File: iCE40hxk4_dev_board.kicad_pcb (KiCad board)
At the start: 4 copper layers, 66.4 x 162.5 mm, 367 parts, among them J1001 Testpoint, J1002 Testpoint, J1003 Testpoint, J1004 Testpoint, J1005 USB_EXT, J101 CONN_01X02, J102 KobiConn_161-3507_Jack_3.5mm, J103 CONN_COAXIAL, J104 CONN_COAXIAL, J1101 CONN_01X25, J202 USB_OTG, J401 Testpoint, J402 Testpoint, J403 Testpoint, J404 Testpoint, J405 Testpoint, J406 Testpoint, J501 Testpoint, J502 Testpoint, J601 CONN_01X02, J602 CONN_01X02, J603 Testpoint, J604 Testpoint, J605 Testpoint, J701 Testpoint, J702 Testpoint, J703 Testpoint, J704 Testpoint, J705 Testpoint, J706 Testpoint, J801 Testpoint, J802 Testpoint, J803 Testpoint, J804 Testpoint, J805 Testpoint, J806 Testpoint, J807 Testpoint, J808 Testpoint, J809 Testpoint, J810 Testpoint, SW1101 SW_Push, U1001 ADC1175, U1002 ADC1175, U1101 MIC7300, U1102 MIC7300, U1103 MCP4716, U1104 MCP4716, U1105 MIC7300, U1106 MIC7300, U201 MIC2005A-2YM5, U203 93LC56BT-I/O, U204 MIC5355/6-xYMME, U205 FT2232H, U301 iCE40-HX4K-TQ144, U302 25LC_EEPROM, U501 AS4C1M16S, U701 CPC1017N, U702 CPC1017N, U703 CD4051BM96, U704 CD4051BM96, U801 CD4051BM96, U802 CD4051BM96, U803 CLC4007, U901 LM2776DBVR, U902 TCR2EF13, U903 MIC5270

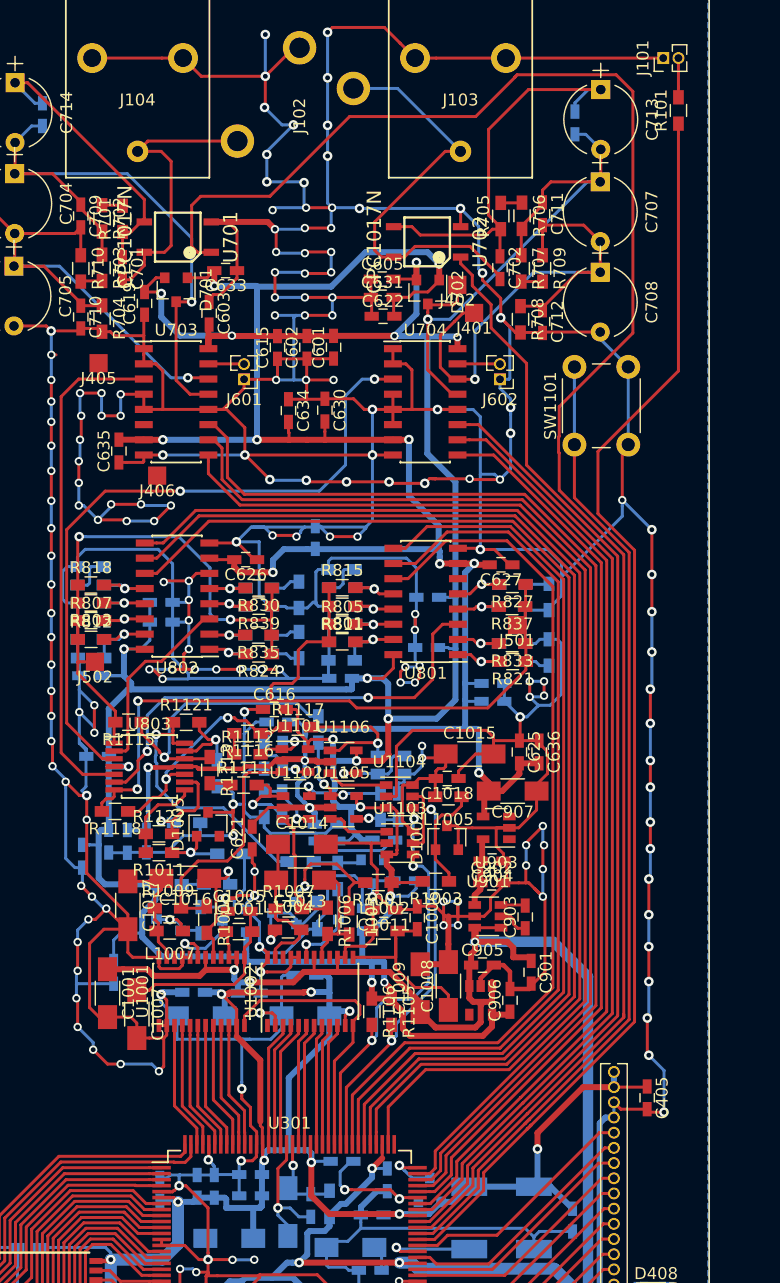
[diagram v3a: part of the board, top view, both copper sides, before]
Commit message: Added resistance to control lines to prevent overshoot
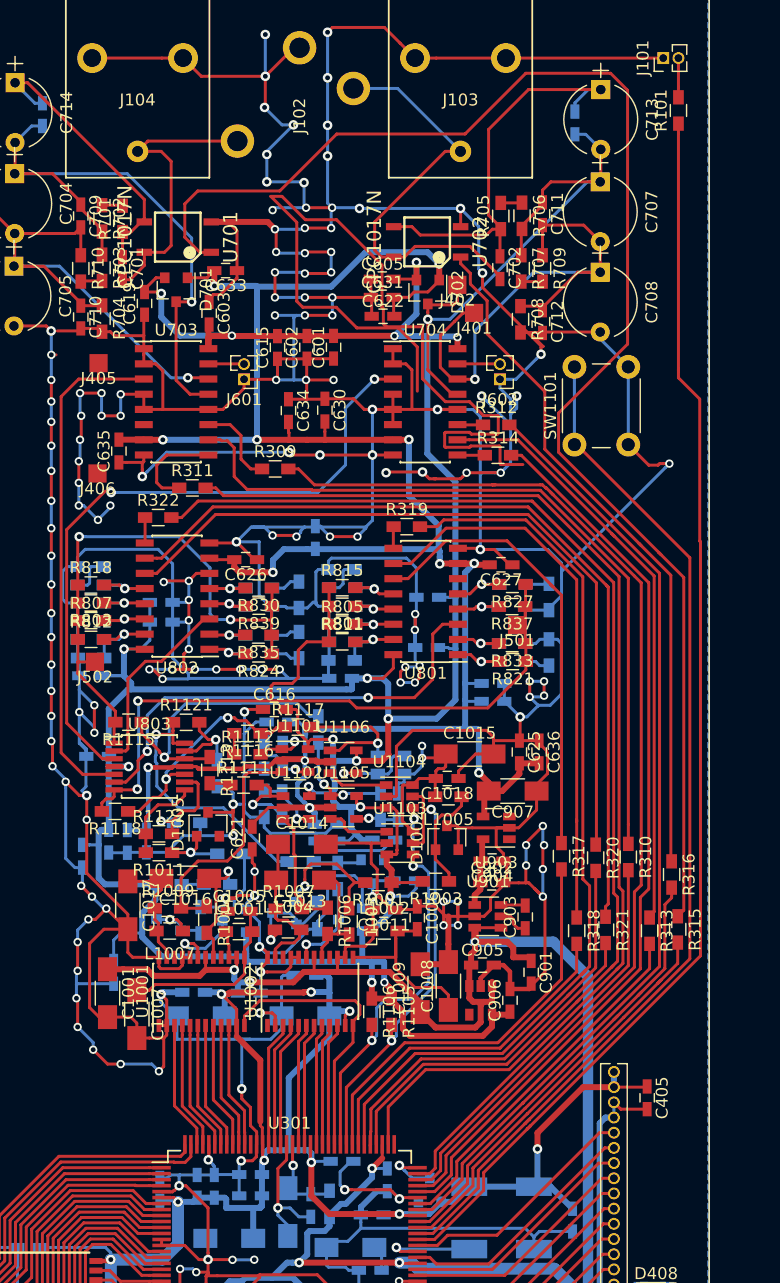
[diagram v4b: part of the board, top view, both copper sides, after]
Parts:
- added R309: 1K, Resistors_SMD:R_0603_HandSoldering, F.Cu at (117.6, 74.3)
- added R310: 1K, Resistors_SMD:R_0603_HandSoldering, F.Cu at (147.2, 106.7)
- added R311: 1K, Resistors_SMD:R_0603_HandSoldering, F.Cu at (110.7, 75.9)
- added R312: 1K, Resistors_SMD:R_0603_HandSoldering, F.Cu at (136.1, 70.6)
- added R313: 1K, Resistors_SMD:R_0603_HandSoldering, F.Cu at (148.9, 112.9)
- added R314: 1K, Resistors_SMD:R_0603_HandSoldering, F.Cu at (136.3, 73.1)
- added R315: 1K, Resistors_SMD:R_0603_HandSoldering, F.Cu at (151.3, 112.8)
- added R316: 1K, Resistors_SMD:R_0603_HandSoldering, F.Cu at (150.8, 108.2)
- added R317: 1K, Resistors_SMD:R_0603_HandSoldering, F.Cu at (141.6, 106.7)
- added R318: 1K, Resistors_SMD:R_0603_HandSoldering, F.Cu at (142.9, 112.9)
- added R319: 1K, Resistors_SMD:R_0603_HandSoldering, F.Cu at (128.6, 79.1)
- added R320: 1K, Resistors_SMD:R_0603_HandSoldering, F.Cu at (144.4, 106.8)
- added R321: 1K, Resistors_SMD:R_0603_HandSoldering, F.Cu at (145.3, 112.8)
- added R322: 1K, Resistors_SMD:R_0603_HandSoldering, F.Cu at (107.9, 78.3)
- moved J406 4.99 mm to (102.8, 74.6)
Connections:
- U701 pad 1: /Analog front end/CHA_DC_COUPLING -> /Analog front end/ATTENUATION/CHA_DC_COUPLING
- U702 pad 1: /Analog front end/CHB_DC_COUPLING -> /Analog front end/ATTENUATION/CHB_DC_COUPLING
- U703 pad 10: /Analog front end/CHA_ATT_SEL_1 -> /Analog front end/ATTENUATION/CHA_ATT_SEL_1
- U703 pad 11: /Analog front end/CHA_ATT_SEL_0 -> /Analog front end/ATTENUATION/CHA_ATT_SEL_0
- U703 pad 9: /Analog front end/CHA_ATT_SEL_2 -> /Analog front end/ATTENUATION/CHA_ATT_SEL_2
- U704 pad 10: /Analog front end/CHB_ATT_SEL_1 -> /Analog front end/ATTENUATION/CHB_ATT_SEL_1
- U704 pad 11: /Analog front end/CHB_ATT_SEL_0 -> /Analog front end/ATTENUATION/CHB_ATT_SEL_0
- U704 pad 9: /Analog front end/CHB_ATT_SEL_2 -> /Analog front end/ATTENUATION/CHB_ATT_SEL_2
- U801 pad 10: /Analog front end/CHA_GAIN_SEL_1 -> /Analog front end/PGA/CHA_GAIN_SEL_1
- U801 pad 11: /Analog front end/CHA_GAIN_SEL_0 -> /Analog front end/PGA/CHA_GAIN_SEL_0
- U801 pad 9: /Analog front end/CHA_GAIN_SEL_2 -> /Analog front end/PGA/CHA_GAIN_SEL_2
- U802 pad 10: /Analog front end/CHB_GAIN_SEL_1 -> /Analog front end/PGA/CHB_GAIN_SEL_1
- U802 pad 11: /Analog front end/CHB_GAIN_SEL_0 -> /Analog front end/PGA/CHB_GAIN_SEL_0
- U802 pad 9: /Analog front end/CHB_GAIN_SEL_2 -> /Analog front end/PGA/CHB_GAIN_SEL_2
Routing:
- net /Analog front end/ATTENUATION/CHA_DC_COUPLING: track 0.00 -> 123.9 mm
- net /Analog front end/CHA_DC_COUPLING: track 155.7 -> 33.9 mm
- net (no net): track 0.00 -> 72.3 mm
- net /Analog front end/PGA/CHB_GAIN_SEL_1: track 0.00 -> 71.6 mm
- net GND: track 1631.9 -> 1560.8 mm, vias 220 -> 197
- net /Analog front end/CHB_GAIN_SEL_1: track 98.5 -> 28.9 mm
- net /Analog front end/PGA/CHB_GAIN_SEL_0: track 0.00 -> 64.5 mm
- net /Analog front end/ATTENUATION/CHA_ATT_SEL_1: track 0.00 -> 63.5 mm
- net /Analog front end/CHB_GAIN_SEL_0: track 98.2 -> 35.2 mm
- net /Analog front end/CHA_ATT_SEL_1: track 95.8 -> 34.0 mm
- net /Analog front end/ATTENUATION/CHB_DC_COUPLING: track 0.00 -> 58.3 mm
- net /Analog front end/CHB_DC_COUPLING: track 93.6 -> 38.1 mm
- net /Analog front end/ATTENUATION/CHB_ATT_SEL_1: track 0.00 -> 50.4 mm
- net /Analog front end/CHB_ATT_SEL_1: track 77.6 -> 30.5 mm
- net /Analog front end/PGA/CHA_GAIN_SEL_1: track 0.00 -> 46.7 mm
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
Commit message: Almost rev1
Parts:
- removed J703, J704: Testpoint, library:TestPoint
- added J105: MountingHole, library:MountingHole, F.Cu at (90.5, 187.0)
- added J106: MountingHole, library:MountingHole, F.Cu at (151.5, 187.0)
- added J107: MountingHole, library:MountingHole, F.Cu at (90.5, 32.0)
- added J108: MountingHole, library:MountingHole, F.Cu at (151.5, 32.0)
- J705, J706, J801, J802, J805, J809, J810: moved to B.Cu
- U203: value 93LC56BT-I/O -> 93LC56BT-I/OT
- U204: value MIC5355/6-xYMME -> MIC5355-S4YMME
- U902: value TCR2EF13 -> TCR2EF13,LM(CT
- moved J403 138.5 mm to (109.3, 62.2)
- moved J702 91.7 mm to (114.9, 108.6)
- moved J808 75.1 mm to (104.2, 105.8)
- moved J807 73.8 mm to (111.6, 93.7)
- moved J1002 70.4 mm to (128.4, 185.9)
- moved J802 68.6 mm to (115.1, 97.9)
- moved J604 66.1 mm to (122.8, 91.3)
- moved J806 65.7 mm to (121.0, 94.2)
- moved J801 62.1 mm to (118.7, 105.0)
- moved J706 61.7 mm to (117.3, 108.9)
- moved J804 58.0 mm to (127.4, 98.5)
- moved J803 56.6 mm to (124.6, 105.6)
- moved J605 56.2 mm to (133.0, 94.6)
- moved J701 55.7 mm to (124.6, 107.4)
- moved J705 54.8 mm to (122.8, 114.0)
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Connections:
- J1005 pad 2: Net-(J1005-Pad2) -> (no net)
- J1005 pad 3: Net-(J1005-Pad3) -> (no net)
- J1005 pad 4: Net-(J1005-Pad4) -> (no net)
- J101 pad 1: GND -> Net-(J101-Pad1)
- J101 pad 2: Net-(J101-Pad2) -> Net-(J101-Pad1)
- J202 pad 4: Net-(J202-Pad4) -> (no net)
- R101 pad 2: Net-(J101-Pad2) -> Net-(J101-Pad1)
- U1001 pad 16: Net-(U1001-Pad16) -> (no net)
- U1001 pad 22: Net-(U1001-Pad22) -> (no net)
- U1002 pad 16: Net-(U1002-Pad16) -> (no net)
- U1002 pad 22: Net-(U1002-Pad22) -> (no net)
- U205 pad 19: Net-(U205-Pad19) -> (no net)
- U205 pad 22: Net-(U205-Pad22) -> (no net)
- U205 pad 26: Net-(U205-Pad26) -> (no net)
- U205 pad 27: Net-(U205-Pad27) -> (no net)
- U205 pad 28: Net-(U205-Pad28) -> (no net)
- U205 pad 29: Net-(U205-Pad29) -> (no net)
- U205 pad 3: Net-(U205-Pad3) -> (no net)
- U205 pad 30: Net-(U205-Pad30) -> (no net)
- U205 pad 32: Net-(U205-Pad32) -> (no net)
- U205 pad 33: Net-(U205-Pad33) -> (no net)
- U205 pad 34: Net-(U205-Pad34) -> (no net)
- U205 pad 36: Net-(U205-Pad36) -> (no net)
- U205 pad 57: Net-(U205-Pad57) -> (no net)
- U205 pad 58: Net-(U205-Pad58) -> (no net)
- U205 pad 59: Net-(U205-Pad59) -> (no net)
- U205 pad 60: Net-(U205-Pad60) -> (no net)
- U301 pad 109: Net-(U301-Pad109) -> (no net)
- U301 pad 133: Net-(U301-Pad133) -> (no net)
- U301 pad 35: Net-(U301-Pad35) -> (no net)
- U301 pad 36: Net-(U301-Pad36) -> (no net)
- U301 pad 50: Net-(U301-Pad50) -> (no net)
- U301 pad 51: Net-(U301-Pad51) -> (no net)
- U301 pad 58: Net-(U301-Pad58) -> (no net)
- U301 pad 77: Net-(U301-Pad77) -> (no net)
- U501 pad 33: Net-(U501-Pad33) -> (no net)
- U501 pad 37: Net-(U501-Pad37) -> (no net)
- U902 pad 4: Net-(U902-Pad4) -> (no net)
- U903 pad 1: Net-(U903-Pad1) -> (no net)
- U903 pad 3: Net-(U903-Pad3) -> (no net)
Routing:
- net (no net): track 72.3 -> 0.00 mm
- net Net-(J101-Pad1): track 0.00 -> 18.6 mm
- net /CHA: track 24.8 -> 37.5 mm
- net /Analog front end/ATTENUATION/CHA_DC_COUPLING: track 123.9 -> 129.5 mm
- net /Analog front end/OFFSET/CHA_V_OFFSET_FIJO: track 4.54 -> 10.0 mm
- net /Analog front end/CHB_OFFSET: track 9.24 -> 14.7 mm
- net /Analog front end/CHB_OFFSET_OUT: track 22.5 -> 27.2 mm
- net /Analog front end/ADC/CHB_V_REF_TOP: track 9.57 -> 13.6 mm
- net /Analog front end/CHB_DC_COUPLING: track 38.1 -> 41.7 mm
- net /Analog front end/-3V0: track 199.1 -> 202.6 mm, vias 12 -> 13
- net /USB+OSCILLATOR+REGULATOR/Vbus_filtered: track 11.8 -> 15.3 mm
- net Net-(J101-Pad2): track 3.28 -> 0.00 mm
- net /RIGHT_TOP_BANKs/IOT_177: track 35.9 -> 39.1 mm
- net /Analog front end/CHA_OFFSET_OUT: track 7.45 -> 10.3 mm
- net /USB+OSCILLATOR+REGULATOR/Vext_filtered: track 33.2 -> 36.0 mm
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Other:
- board size 66.4 x 162.5 mm -> 67 x 161 mm
- board text added: "2017"
- board text added: "N. Carducci A. Demski A. Kukulanski I. Paunovic"
- board text added: "SMARTBENCH"
- board text added: "mainboard"
- board text added: "rev 1"

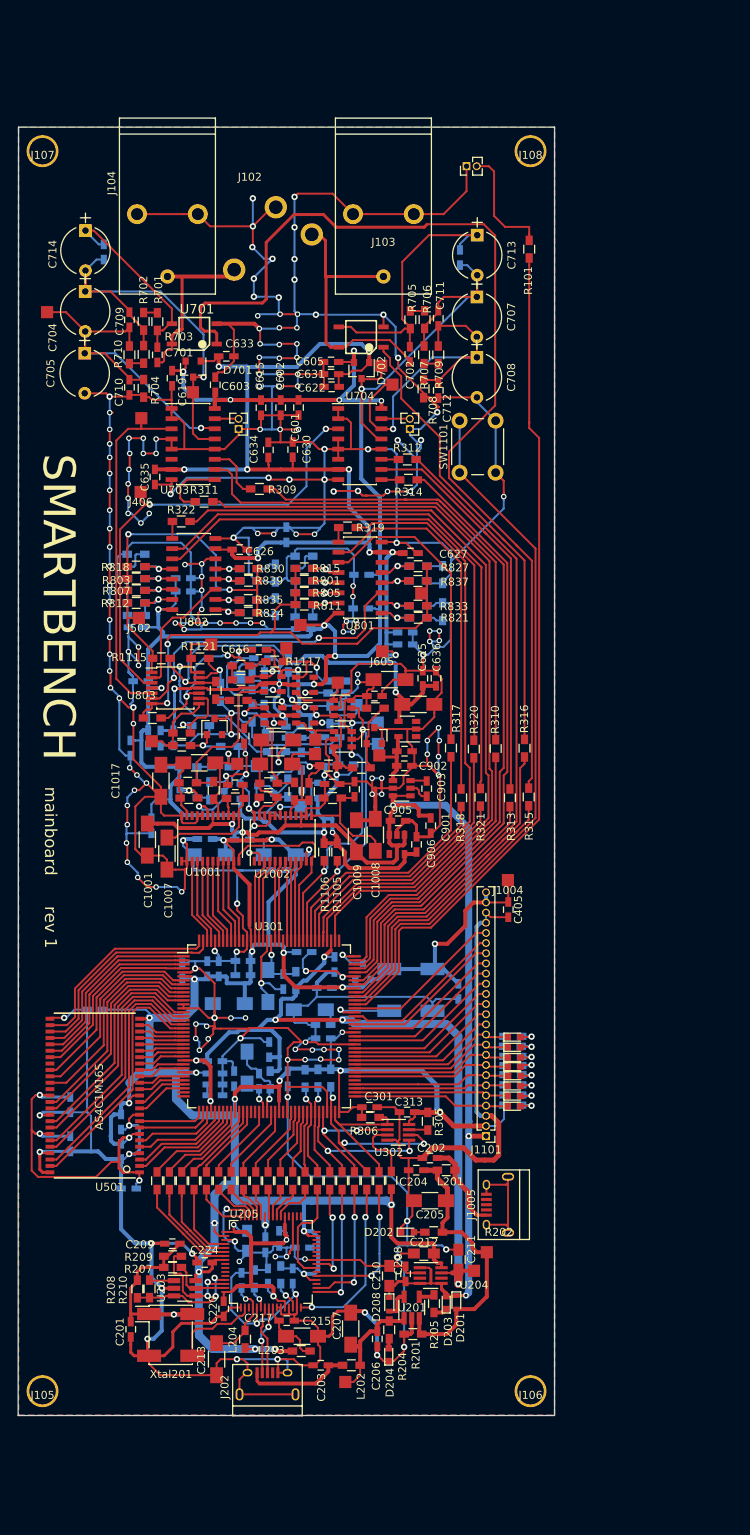
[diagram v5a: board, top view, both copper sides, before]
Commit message: Corrected digital part of pcb with new footprints of roms and new oscillators
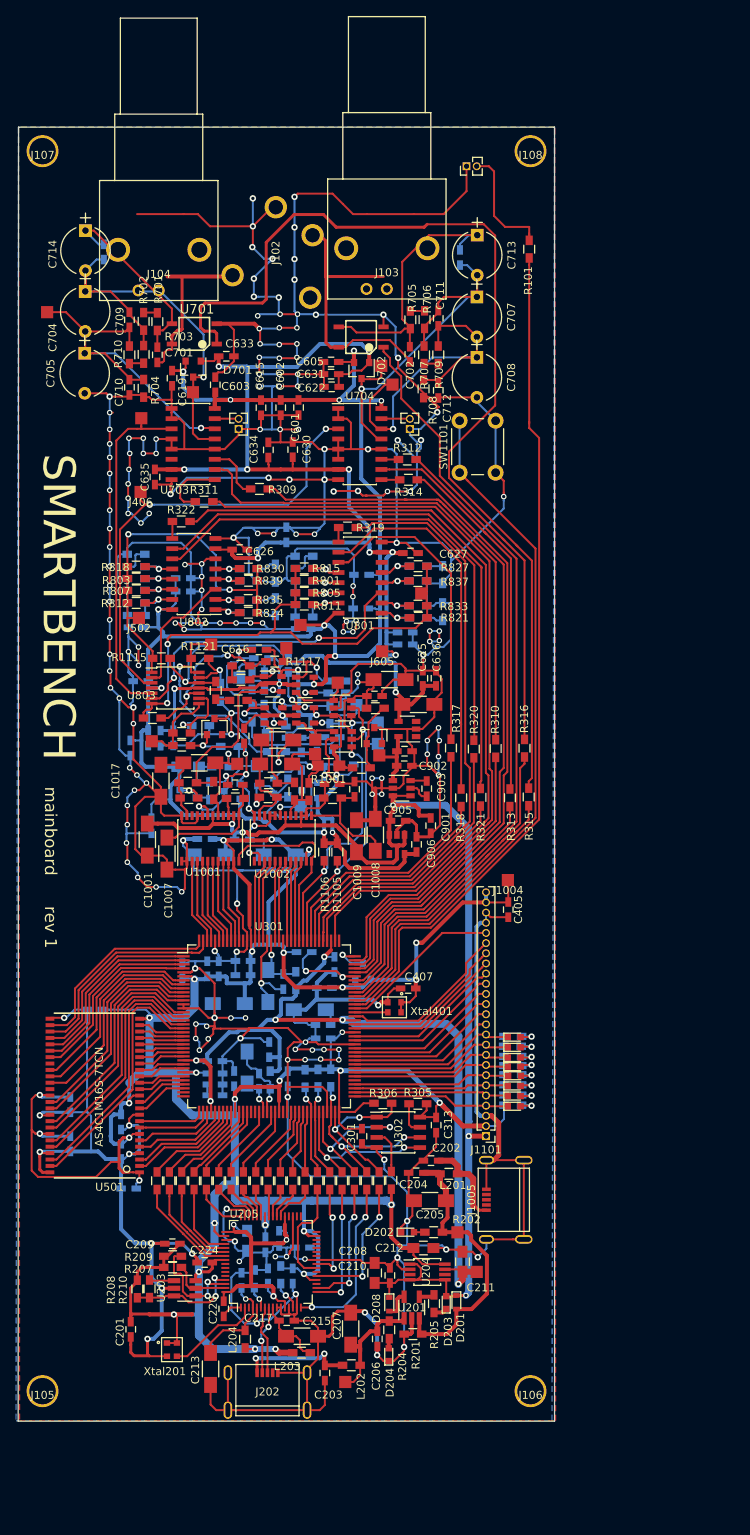
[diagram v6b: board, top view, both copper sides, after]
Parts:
- C407: moved to F.Cu
- C709, C711: value 180p -> 180pF
- C710, C712: value 1800p -> 1800pF
- J1005, J202: footprint Connectors:USB_Micro-B -> library:USB_Micro-B_47642-0001
- J102: value KobiConn_161-3507_Jack_3.5mm -> Jack Estereo; footprint library:KobiConn_161-3507_Jack_3.5mm -> library:KobiConn_161-3509-E_Jack_3.5mm
- J103, J104: footprint library:Molex_73100-0105_BNC -> library:BNC_1-1337543-0
- R1001, R1004: footprint Resistors_SMD:R_0603_HandSoldering -> Resistors_SMD:R_0805_HandSoldering
- R703, R707: value 89K8 -> 90K9
- U204: footprint TO_SOT_Packages_SMD:SOT-23-8_Handsoldering -> Housings_SSOP:MSOP-8_3x3mm_Pitch0.65mm
- U302: value 25LC_EEPROM -> FLASH 2Mb; footprint TO_SOT_Packages_SMD:SOT-23-8_Handsoldering -> Housings_SOIC:SOIC-8_3.9x4.9mm_Pitch1.27mm
- U501: value AS4C1M16S -> AS4C1M16S-7TCN
- U902: value TCR2EF13,LM(CT -> TCR2EF13,LM
- Xtal201: footprint Oscillators:Oscillator_SMD_Fordahl_DFAS11-4pin_7.0x5.0mm_HandSoldering -> library:VLGA_4_2.5x2.0mm
- Xtal401: footprint Oscillators:Oscillator_SMD_Fordahl_DFAS11-4pin_7.0x5.0mm_HandSoldering -> library:VLGA_4_2.5x2.0mm; moved to F.Cu
- moved C407 6.29 mm to (136.2, 136.7), turned to 180 degrees
- moved J1001 4.44 mm to (142.4, 167.2)
- moved C313 3.98 mm to (139.7, 153.8), turned to 270 degrees
- moved C301 3.75 mm to (130.5, 155.2), turned to 270 degrees
- moved J104 3.19 mm to (105.1, 46.9), turned to 0 degrees
- moved Xtal401 2.99 mm to (134.5, 139.1), turned to 180 degrees
- moved J103 2.84 mm to (133.6, 46.7), turned to 0 degrees
- moved R305 2.51 mm to (137.4, 151.1), turned to 180 degrees
- moved R306 2.35 mm to (133.1, 151.1)
- moved C208 1.97 mm to (133.9, 172.6)
- moved C210 1.87 mm to (132.0, 172.3)
- moved Xtal201 1.85 mm to (106.7, 181.9)
- moved C213 1.43 mm to (111.5, 184.3)
- moved C203 1.09 mm to (125.8, 184.8), turned to 270 degrees
- moved C212 0.69 mm to (138.1, 169.2), turned to 0 degrees
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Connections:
- J1005 pad 2: (no net) -> Net-(J1005-Pad2)
- J1005 pad 3: (no net) -> Net-(J1005-Pad3)
- J1005 pad 4: (no net) -> Net-(J1005-Pad4)
- J202 pad 4: (no net) -> Net-(J202-Pad4)
- U1001 pad 16: (no net) -> Net-(U1001-Pad16)
- U1001 pad 22: (no net) -> Net-(U1001-Pad22)
- U1002 pad 16: (no net) -> Net-(U1002-Pad16)
- U1002 pad 22: (no net) -> Net-(U1002-Pad22)
- U205 pad 19: (no net) -> Net-(U205-Pad19)
- U205 pad 22: (no net) -> Net-(U205-Pad22)
- U205 pad 26: (no net) -> Net-(U205-Pad26)
- U205 pad 27: (no net) -> Net-(U205-Pad27)
- U205 pad 28: (no net) -> Net-(U205-Pad28)
- U205 pad 29: (no net) -> Net-(U205-Pad29)
- U205 pad 3: (no net) -> Net-(U205-Pad3)
- U205 pad 30: (no net) -> Net-(U205-Pad30)
- U205 pad 32: (no net) -> Net-(U205-Pad32)
- U205 pad 33: (no net) -> Net-(U205-Pad33)
- U205 pad 34: (no net) -> Net-(U205-Pad34)
- U205 pad 36: (no net) -> Net-(U205-Pad36)
- U205 pad 57: (no net) -> Net-(U205-Pad57)
- U205 pad 58: (no net) -> Net-(U205-Pad58)
- U205 pad 59: (no net) -> Net-(U205-Pad59)
- U205 pad 60: (no net) -> Net-(U205-Pad60)
- U301 pad 109: (no net) -> Net-(U301-Pad109)
- U301 pad 133: (no net) -> Net-(U301-Pad133)
- U301 pad 35: (no net) -> Net-(U301-Pad35)
- U301 pad 36: (no net) -> Net-(U301-Pad36)
- U301 pad 50: (no net) -> Net-(U301-Pad50)
- U301 pad 51: (no net) -> Net-(U301-Pad51)
- U301 pad 58: (no net) -> Net-(U301-Pad58)
- U301 pad 77: (no net) -> Net-(U301-Pad77)
- U501 pad 33: (no net) -> Net-(U501-Pad33)
- U501 pad 37: (no net) -> Net-(U501-Pad37)
- U902 pad 4: (no net) -> Net-(U902-Pad4)
- U903 pad 1: (no net) -> Net-(U903-Pad1)
- U903 pad 3: (no net) -> Net-(U903-Pad3)
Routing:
- net GND: track 1562.7 -> 1530.3 mm, vias 198 -> 199
- net +3V3: track 497.8 -> 507.6 mm, vias 29 -> 30
- net Net-(J101-Pad1): track 18.6 -> 26.4 mm
- net /CHA: track 37.5 -> 45.1 mm
- net /Analog front end/ATTENUATION/CHA_ATT_20dB: track 51.1 -> 43.5 mm
- net /RIGHT_TOP_BANKs/OSC: track 8.06 -> 4.15 mm, vias 1 -> 0
- net +5V: track 160.0 -> 163.7 mm
- net /FPGA_PROGRAMMING+POWER/SCK: track 25.8 -> 23.5 mm
- net Net-(R304-Pad2): track 7.92 -> 5.63 mm
- net Net-(C213-Pad1): track 10.9 -> 13.0 mm
- net /FPGA_PROGRAMMING+POWER/MISO: track 17.6 -> 19.5 mm
- net Net-(R305-Pad2): track 2.36 -> 4.10 mm
- net Net-(C203-Pad1): track 13.3 -> 14.4 mm, vias 0 -> 2
- net /USB+OSCILLATOR+REGULATOR/Vext_filtered: track 36.0 -> 35.2 mm
- net /RIGHT_TOP_BANKs/IOR_140: track 20.9 -> 21.7 mm
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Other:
- board size 67 x 161 mm -> 67 x 161.8 mm
